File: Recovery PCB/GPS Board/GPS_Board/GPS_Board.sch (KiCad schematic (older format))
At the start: 16 parts, among them J1 XT30-M, J2 XT30-M, U1 Teensy4.1, U2 D24V22F5_VoltageRegulator, U3 LD1117v33

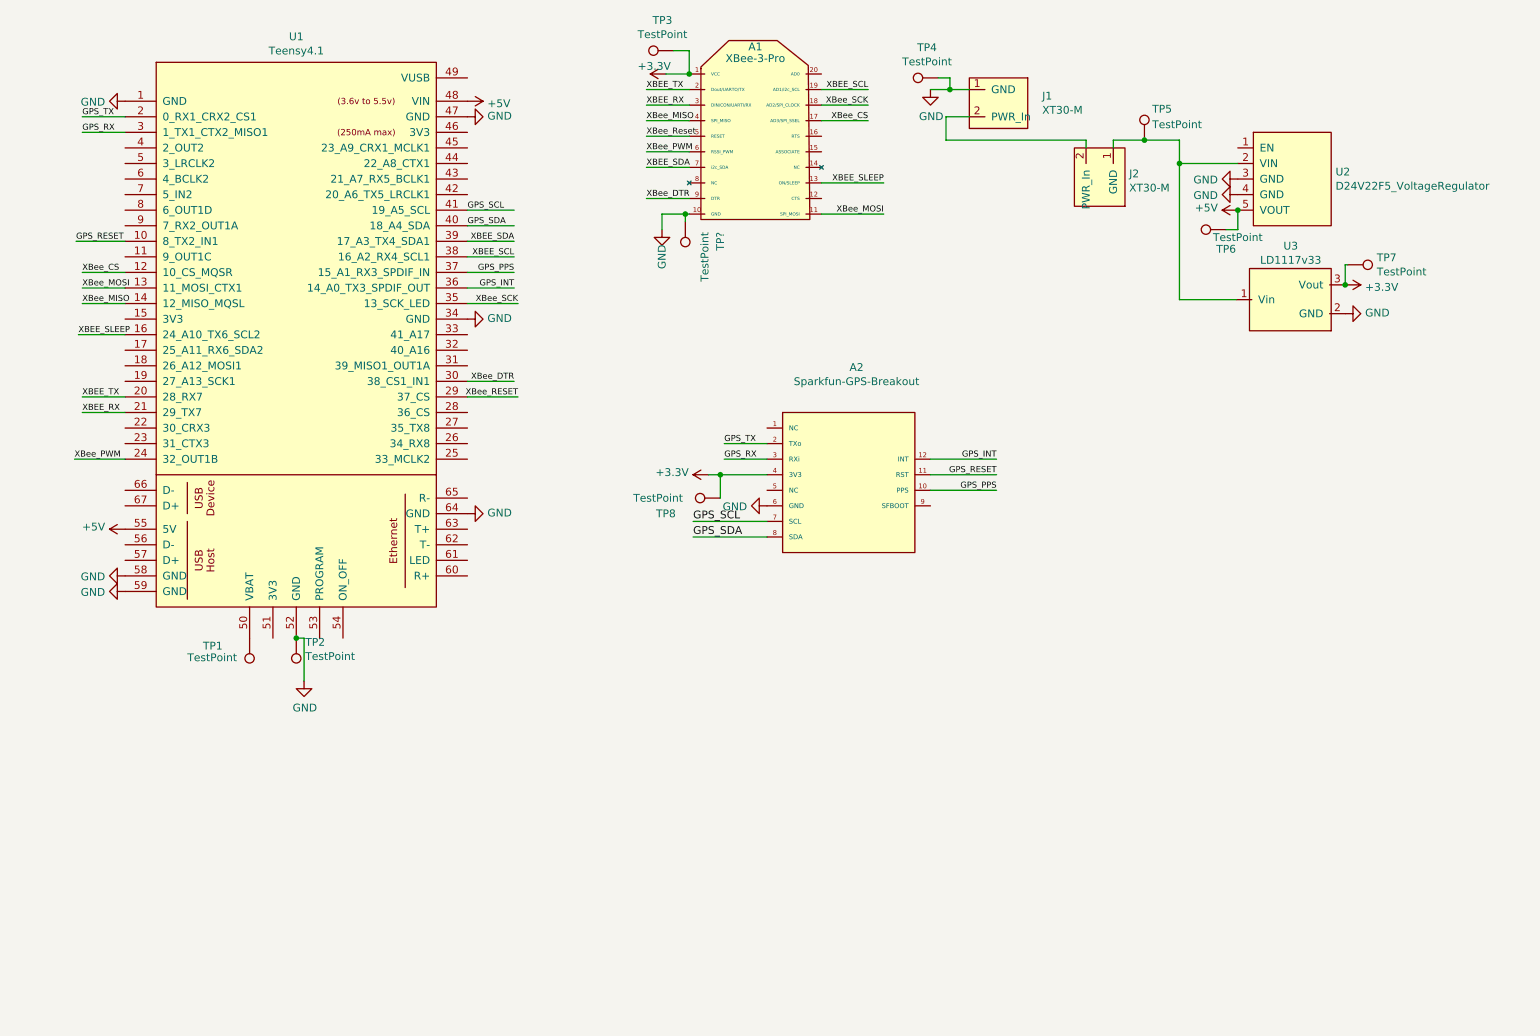
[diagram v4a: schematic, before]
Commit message: Added connectors and updated traces.
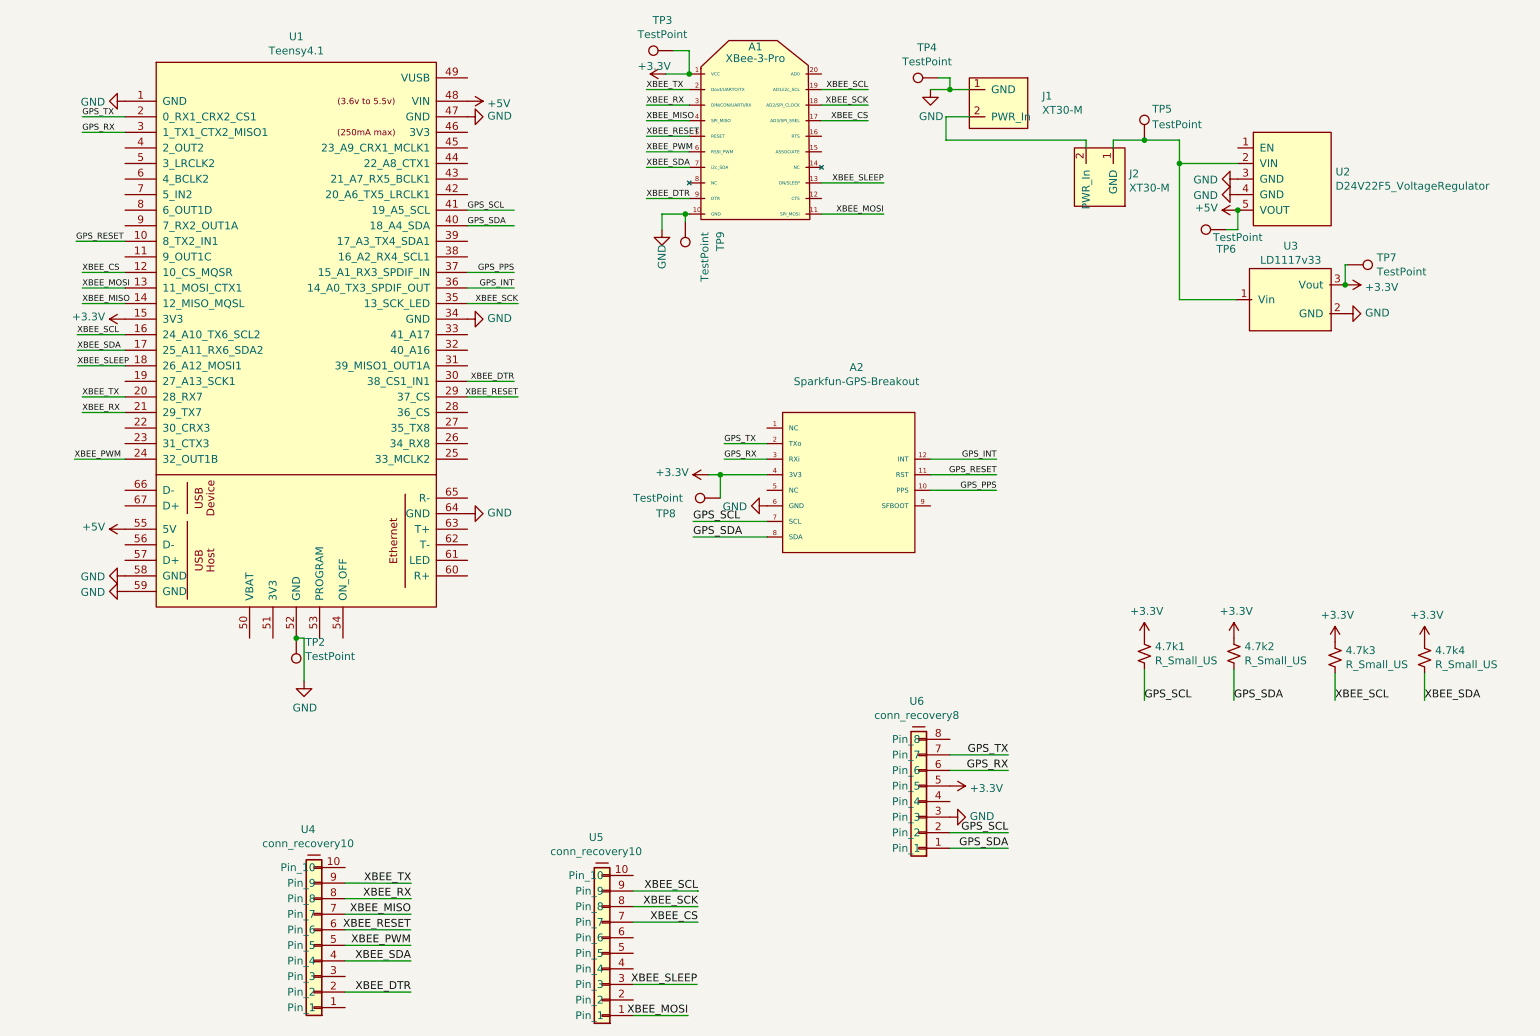
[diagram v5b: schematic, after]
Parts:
- removed TP1: TestPoint, TestPoint:TestPoint_Pad_D2.0mm, symbol Connector:TestPoint
- added 4.7k1, 4.7k2, 4.7k3, 4.7k4: R_Small_US, GPS Board:0603, symbol Device:R_Small_US
- added U4, U5: conn_recovery10, Connector_PinHeader_2.54mm:PinHeader_1x10_P2.54mm_Vertical, symbol GPS_Board:conn_recovery10
- added U6: conn_recovery8, Connector_PinHeader_2.54mm:PinHeader_1x08_P2.54mm_Vertical, symbol GPS_Board:conn_recovery8
- TP8: footprint (none) -> TestPoint:TestPoint_Pad_D2.0mm
- gave numbers to parts that had none: 1
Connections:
- net XBee_Reset is gone; now on net XBEE_RESET: A1.5 (RESET)
- net +3V3: now also U1.15 (3V3), 4.7k1.1, 4.7k2.1, 4.7k3.1, 4.7k4.1, U6.5 (Pin_5)
- net GND: now also U6.3 (Pin_3)
- net GPS_RX: now also U6.6 (Pin_6)
- net GPS_SCL: now also 4.7k1.2, U6.2 (Pin_2)
- net GPS_SDA: now also 4.7k2.2, U6.1 (Pin_1)
- net GPS_TX: now also U6.7 (Pin_7)
- net XBEE_RX: now also U4.8 (Pin_8)
- net XBEE_SCL: now also U1.16 (24_A10_TX6_SCL2), 4.7k3.2, U5.9 (Pin_9); no longer U1.38 (16_A2_RX4_SCL1)
- net XBEE_SDA: now also U1.17 (25_A11_RX6_SDA2), 4.7k4.2, U4.4 (Pin_4); no longer U1.39 (17_A3_TX4_SDA1)
- net XBEE_SLEEP: now also U1.18 (26_A12_MOSI1), U5.3 (Pin_3); no longer U1.16 (24_A10_TX6_SCL2)
- net XBEE_TX: now also U4.9 (Pin_9)
- net XBee_CS renamed XBEE_CS
- net XBEE_CS: now also U5.7 (Pin_7)
- net XBee_DTR renamed XBEE_DTR
- net XBEE_DTR: now also U4.2 (Pin_2)
- net XBee_MISO renamed XBEE_MISO
- net XBEE_MISO: now also U4.7 (Pin_7)
- net XBee_MOSI renamed XBEE_MOSI
- net XBEE_MOSI: now also U5.1 (Pin_1)
- net XBee_PWM renamed XBEE_PWM
- net XBEE_PWM: now also U4.5 (Pin_5)
- net XBee_RESET renamed XBEE_RESET
- net XBEE_RESET: now also U4.6 (Pin_6)
- net XBee_SCK renamed XBEE_SCK
- net XBEE_SCK: now also U5.8 (Pin_8)

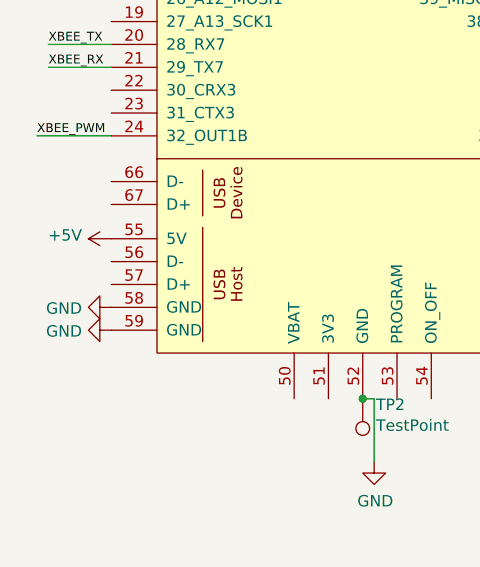
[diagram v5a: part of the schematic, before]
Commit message: Created SMD Breakout Pins
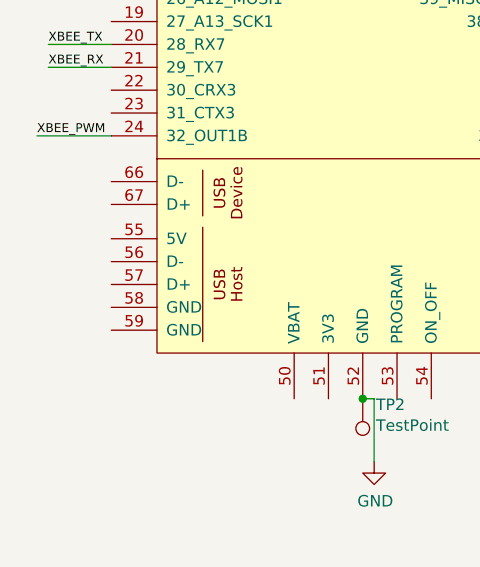
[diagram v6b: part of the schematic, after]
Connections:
- net +5V: no longer U1.55 (5V)
- net GND: no longer U1.58 (GND), U1.59 (GND)
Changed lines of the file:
@@
 GPS_RX
-$Comp
-L power:GND #PWR0117
-U 1 1 625EB8C1
-P 1800 4550
-F 0 "#PWR0117" H 1800 4300 50  0001 C CNN
-F 1 "GND" V 1805 4422 50  0000 R CNN
-F 2 "" H 1800 4550 50  0001 C CNN
-F 3 "" H 1800 4550 50  0001 C CNN
-	1    1800 4550
-	0    1    1    0
-$EndComp
-$Comp
-L power:GND #PWR0118
-U 1 1 625EC4CE
-P 1800 4450
-F 0 "#PWR0118" H 1800 4200 50  0001 C CNN
-F 1 "GND" V 1805 4322 50  0000 R CNN
-F 2 "" H 1800 4450 50  0001 C CNN
-F 3 "" H 1800 4450 50  0001 C CNN
-	1    1800 4450
-	0    1    1    0
-$EndComp
-$Comp
-L power:+5V #PWR0119
-U 1 1 625ECDBB
-P 1800 4150
-F 0 "#PWR0119" H 1800 4000 50  0001 C CNN
-F 1 "+5V" V 1815 4278 50  0000 L CNN
-F 2 "" H 1800 4150 50  0001 C CNN
-F 3 "" H 1800 4150 50  0001 C CNN
-	1    1800 4150
-	0    -1   -1   0
-$EndComp
 $Comp
 L power:GND #PWR0121

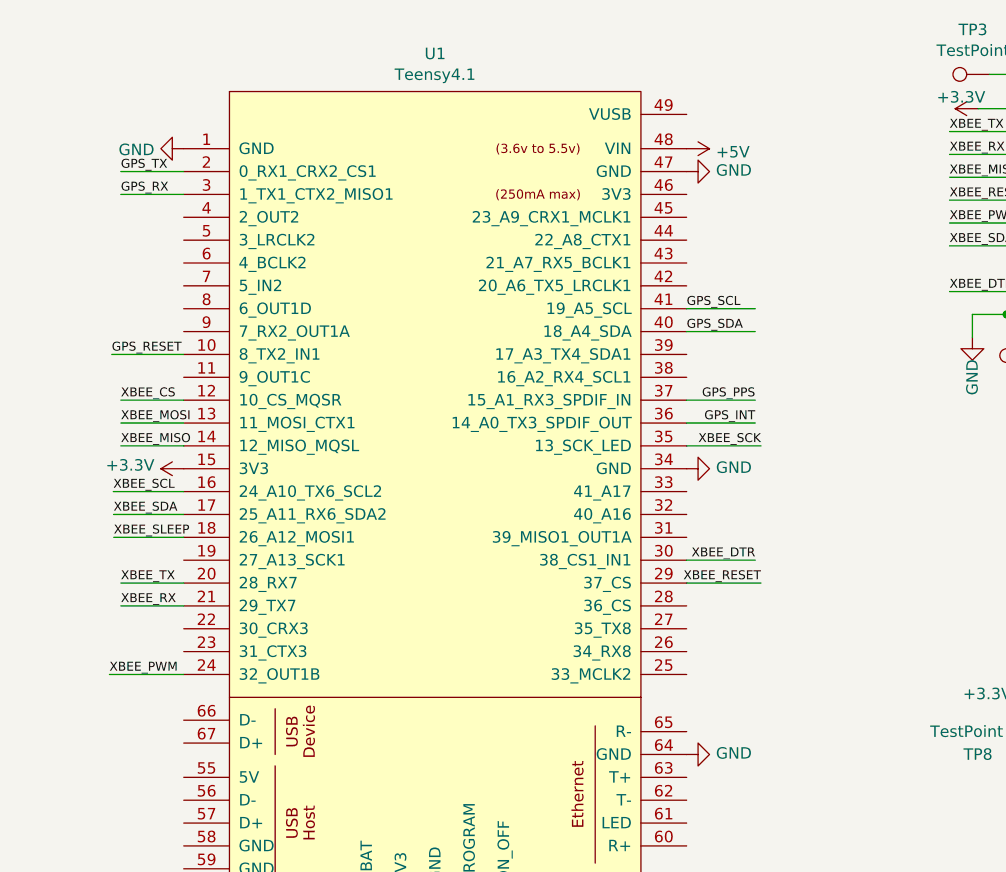
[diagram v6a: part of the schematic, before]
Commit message: Added teensy breakout pads
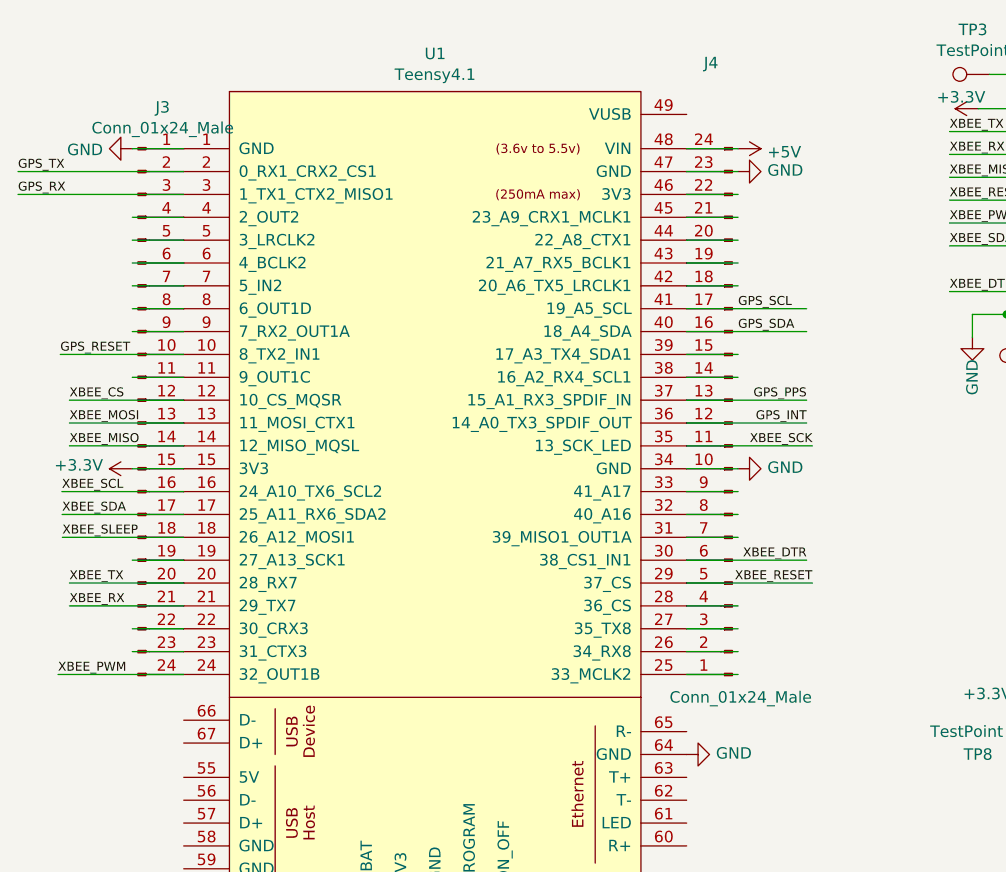
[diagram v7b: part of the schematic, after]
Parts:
- added J3, J4: Conn_01x24_Male, GPS Board:SMD_Connector_1x24, symbol Connector:Conn_01x24_Male
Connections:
- wire segments 90 -> 119
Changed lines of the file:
@@
 L power:GND #PWR0102
 U 1 1 61ABF5FF
-P 1800 1400
-F 0 "#PWR0102" H 1800 1150 50  0001 C CNN
-F 1 "GND" V 1805 1272 50  0000 R CNN
-F 2 "" H 1800 1400 50  0001 C CNN
-F 3 "" H 1800 1400 50  0001 C CNN
-	1    1800 1400
+P 1575 1400
+F 0 "#PWR0102" H 1575 1150 50  0001 C CNN
+F 1 "GND" V 1580 1272 50  0000 R CNN
+F 2 "" H 1575 1400 50  0001 C CNN
+F 3 "" H 1575 1400 50  0001 C CNN
+	1    1575 1400
 	0    1    1    0
 $EndComp
@@
 L power:GND #PWR0103
 U 1 1 61AC06CC
-P 4000 1500
-F 0 "#PWR0103" H 4000 1250 50  0001 C CNN
-F 1 "GND" V 4005 1372 50  0000 R CNN
-F 2 "" H 4000 1500 50  0001 C CNN
-F 3 "" H 4000 1500 50  0001 C CNN
-	1    4000 1500
+P 4225 1500
+F 0 "#PWR0103" H 4225 1250 50  0001 C CNN
+F 1 "GND" V 4230 1372 50  0000 R CNN
+F 2 "" H 4225 1500 50  0001 C CNN
+F 3 "" H 4225 1500 50  0001 C CNN
+	1    4225 1500
 	0    -1   -1   0
 $EndComp
@@
 L power:GND #PWR0105
 U 1 1 61AC2FBA
-P 4000 2800
-F 0 "#PWR0105" H 4000 2550 50  0001 C CNN
-F 1 "GND" V 4005 2672 50  0000 R CNN
-F 2 "" H 4000 2800 50  0001 C CNN
-F 3 "" H 4000 2800 50  0001 C CNN
-	1    4000 2800
+P 4225 2800
+F 0 "#PWR0105" H 4225 2550 50  0001 C CNN
+F 1 "GND" V 4230 2672 50  0000 R CNN
+F 2 "" H 4225 2800 50  0001 C CNN
+F 3 "" H 4225 2800 50  0001 C CNN
+	1    4225 2800
 	0    -1   -1   0
 $EndComp
@@
 L power:+5V #PWR0107
 U 1 1 61AD1665
-P 4000 1400
-F 0 "#PWR0107" H 4000 1250 50  0001 C CNN
-F 1 "+5V" V 4015 1528 50  0000 L CNN
-F 2 "" H 4000 1400 50  0001 C CNN
-F 3 "" H 4000 1400 50  0001 C CNN
-	1    4000 1400
+P 4225 1400
+F 0 "#PWR0107" H 4225 1250 50  0001 C CNN
+F 1 "+5V" V 4240 1528 50  0000 L CNN
+F 2 "" H 4225 1400 50  0001 C CNN
+F 3 "" H 4225 1400 50  0001 C CNN
+	1    4225 1400
 	0    1    1    0
 $EndComp
@@
 	1    0    0    -1
 $EndComp
-Wire Wire Line
-	4000 2200 4300 2200
 Text Label 5450 4100 0    50   ~ 0
 GPS_SCL
 Text Label 5450 4200 0    50   ~ 0
 GPS_SDA
-Wire Wire Line
-	4000 2100 4300 2100
 $Comp
 L power:+3.3V #PWR0104
@@
 	0    -1   -1   0
 $EndComp
-Text Label 1485 2300 0    39   ~ 0
-GPS_RESET
-Wire Wire Line
-	1800 2300 1485 2300
 Text Label 7400 3800 2    39   ~ 0
 GPS_RESET
@@
 Wire Wire Line
 	6975 3900 7400 3900
-Text Label 4300 2500 2    39   ~ 0
+Text Label 4525 2500 2    39   ~ 0
 GPS_PPS
-Wire Wire Line
-	4000 2500 4300 2500
 Text Label 7400 3900 2    39   ~ 0
 GPS_PPS
-Wire Wire Line
-	4000 2600 4300 2600
-Text Label 4300 2600 2    39   ~ 0
+Text Label 4525 2600 2    39   ~ 0
 GPS_INT
 Text Label 7400 3700 2    39   ~ 0
 GPS_INT
-Text Label 4325 2700 2    39   ~ 0
+Text Label 4550 2700 2    39   ~ 0
 XBEE_SCK
-Wire Wire Line
-	4000 2700 4325 2700
 Text Label 6575 1425 2    39   ~ 0
 XBEE_SCK
-Text Label 1525 2500 0    39   ~ 0
-XBEE_CS
-Wire Wire Line
-	1525 2500 1800 2500
 $Comp
 L power:+3.3V #PWR0108
@@
 	0    -1   -1   0
 $EndComp
-Text Label 1525 2700 0    39   ~ 0
-XBEE_MISO
-Wire Wire Line
-	1800 2700 1525 2700
-Wire Wire Line
-	4000 3300 4325 3300
-Text Label 4325 3300 2    39   ~ 0
+Text Label 4550 3300 2    39   ~ 0
 XBEE_RESET
 Text Label 5150 1725 0    39   ~ 0
 XBEE_PWM
-Wire Wire Line
-	1800 3700 1475 3700
-Text Label 1475 3700 0    39   ~ 0
-XBEE_PWM
 Text Label 5150 2025 0    39   ~ 0
 XBEE_DTR
-Wire Wire Line
-	4000 3200 4300 3200
-Text Label 4300 3200 2    39   ~ 0
+Text Label 4525 3200 2    39   ~ 0
 XBEE_DTR
-Text Label 1494 3100 0    39   ~ 0
-XBEE_SLEEP
 Text Label 6675 2125 2    39   ~ 0
 XBEE_MOSI
@@
 	1    0    0    -1
 $EndComp
-Wire Wire Line
-	1800 2600 1525 2600
-Text Label 1525 2600 0    39   ~ 0
-XBEE_MOSI
 Text Label 6575 1525 2    39   ~ 0
 XBEE_CS
@@
 XBEE_SDA
 Text Label 6575 1325 2    39   ~ 0
-XBEE_SCL
-Text Label 1493 3000 0    39   ~ 0
-XBEE_SDA
-Text Label 1492 2900 0    39   ~ 0
 XBEE_SCL
 Text Label 6675 1925 2    39   ~ 0
@@
 Text Label 5150 1425 0    39   ~ 0
 XBEE_RX
-Wire Wire Line
-	1800 1500 1525 1500
-Wire Wire Line
-	1800 1600 1525 1600
-Text Label 1525 1500 0    39   ~ 0
-GPS_TX
-Text Label 1525 1600 0    39   ~ 0
-GPS_RX
 $Comp
 L power:GND #PWR0121
@@
 Wire Wire Line
 	8350 1650 8575 1650
-Text Label 4000 2100 0    39   ~ 0
+Text Label 4225 2100 0    39   ~ 0
 GPS_SCL
-Text Label 4000 2200 0    39   ~ 0
+Text Label 4225 2200 0    39   ~ 0
 GPS_SDA
 Wire Wire Line
@@
 Connection ~ 9640 2580
 Connection ~ 2900 4850
-Text Label 1525 3400 0    39   ~ 0
-XBEE_RX
-Text Label 1525 3300 0    39   ~ 0
-XBEE_TX
-Wire Wire Line
-	1800 3400 1525 3400
-Wire Wire Line
-	1800 3300 1525 3300
 $Comp
 L GPS_Board-rescue:Teensy4.1-teensy U1
@@
 L power:+3.3V #PWR0126
 U 1 1 62864185
-P 1800 2800
-F 0 "#PWR0126" H 1800 2650 50  0001 C CNN
-F 1 "+3.3V" V 1815 2928 50  0000 L CNN
-F 2 "" H 1800 2800 50  0001 C CNN
-F 3 "" H 1800 2800 50  0001 C CNN
-	1    1800 2800
-	0    -1   -1   0
-$EndComp
-Wire Wire Line
-	1492 2900 1800 2900
-Wire Wire Line
-	1493 3000 1800 3000
-Wire Wire Line
-	1494 3100 1800 3100
+P 1575 2800
+F 0 "#PWR0126" H 1575 2650 50  0001 C CNN
+F 1 "+3.3V" V 1590 2928 50  0000 L CNN
+F 2 "" H 1575 2800 50  0001 C CNN
+F 3 "" H 1575 2800 50  0001 C CNN
+	1    1575 2800
+	0    -1   -1   0
+$EndComp
+Text Label 1300 3300 0    39   ~ 0
+XBEE_TX
+Text Label 1300 3400 0    39   ~ 0
+XBEE_RX
+Text Label 1075 1600 0    39   ~ 0
+GPS_RX
+Text Label 1075 1500 0    39   ~ 0
+GPS_TX
+Text Label 1267 2900 0    39   ~ 0
+XBEE_SCL
+Text Label 1268 3000 0    39   ~ 0
+XBEE_SDA
+Text Label 1300 2600 0    39   ~ 0
+XBEE_MOSI
+Text Label 1269 3100 0    39   ~ 0
+XBEE_SLEEP
+Text Label 1250 3700 0    39   ~ 0
+XBEE_PWM
+Text Label 1300 2700 0    39   ~ 0
+XBEE_MISO
+Text Label 1300 2500 0    39   ~ 0
+XBEE_CS
+Text Label 1260 2300 0    39   ~ 0
+GPS_RESET
+$Comp
+L Connector:Conn_01x24_Male J3
+U 1 1 625F67AB
+P 1600 2500
+F 0 "J3" H 1708 3781 50  0000 C CNN
+F 1 "Conn_01x24_Male" H 1708 3690 50  0000 C CNN
+F 2 "GPS Board:SMD_Connector_1x24" H 1600 2500 50  0001 C CNN
+F 3 "~" H 1600 2500 50  0001 C CNN
+	1    1600 2500
+	1    0    0    -1
+$EndComp
+Wire Wire Line
+	1800 1700 1575 1700
+Wire Wire Line
+	1800 1800 1575 1800
+Wire Wire Line
+	1800 1900 1575 1900
+Wire Wire Line
+	1800 2000 1575 2000
+Wire Wire Line
+	1800 2100 1575 2100
+Wire Wire Line
+	1800 2200 1575 2200
+Wire Wire Line
+	1800 2400 1575 2400
+Wire Wire Line
+	1800 2800 1575 2800
+Wire Wire Line
+	1800 3200 1575 3200
+Wire Wire Line
+	1800 3500 1575 3500
+Wire Wire Line
+	1800 3600 1575 3600
+Wire Wire Line
+	1269 3100 1800 3100
+Wire Wire Line
+	1268 3000 1800 3000
+Wire Wire Line
+	1267 2900 1800 2900
+Wire Wire Line
+	1300 3300 1800 3300
+Wire Wire Line
+	1300 3400 1800 3400
+Wire Wire Line
+	1300 2600 1800 2600
+Wire Wire Line
+	1250 3700 1800 3700
+Wire Wire Line
+	1300 2700 1800 2700
+Wire Wire Line
+	1300 2500 1800 2500
+Wire Wire Line
+	1260 2300 1800 2300
+$Comp
+L Connector:Conn_01x24_Male J4
+U 1 1 62662A48
+P 4200 2600
+F 0 "J4" H 4325 1025 50  0000 R CNN
+F 1 "Conn_01x24_Male" H 4475 3800 50  0000 R CNN
+F 2 "GPS Board:SMD_Connector_1x24" H 4200 2600 50  0001 C CNN
+F 3 "~" H 4200 2600 50  0001 C CNN
+	1    4200 2600
+	-1   0    0    1
+$EndComp
+Wire Wire Line
+	4000 1400 4225 1400
+Wire Wire Line
+	4225 1500 4000 1500
+Wire Wire Line
+	4000 1600 4225 1600
+Wire Wire Line
+	1800 1400 1575 1400
+Wire Wire Line
+	1075 1600 1800 1600
+Wire Wire Line
+	1075 1500 1800 1500
+Wire Wire Line
+	4000 1700 4225 1700
+Wire Wire Line
+	4225 1800 4000 1800
+Wire Wire Line
+	4000 1900 4225 1900
+Wire Wire Line
+	4000 2000 4225 2000
+Wire Wire Line
+	4000 2300 4225 2300
+Wire Wire Line
+	4225 2400 4000 2400
+Wire Wire Line
+	4000 2800 4225 2800
+Wire Wire Line
+	4000 2900 4225 2900
+Wire Wire Line
+	4225 3000 4000 3000
+Wire Wire Line
+	4000 3100 4225 3100
+Wire Wire Line
+	4000 3400 4225 3400
+Wire Wire Line
+	4000 3500 4225 3500
+Wire Wire Line
+	4225 3600 4000 3600
+Wire Wire Line
+	4000 3700 4225 3700
+Wire Wire Line
+	4000 2200 4525 2200
+Wire Wire Line
+	4000 2100 4525 2100
+Wire Wire Line
+	4000 2500 4525 2500
+Wire Wire Line
+	4000 2600 4525 2600
+Wire Wire Line
+	4000 2700 4550 2700
+Wire Wire Line
+	4000 3300 4550 3300
+Wire Wire Line
+	4000 3200 4525 3200
 $EndSCHEMATC
